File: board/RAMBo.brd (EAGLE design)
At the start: 104.1 x 102.9 mm, 273 parts, among them Q1 PSMN7R0-60YS, Q2 PSMN7R0-60YS, Q3 PSMN7R0-60YS, Q4 IRLML6346TRPBF, Q5 PSMN7R0-60YS, Q8 IRLML6346TRPBF, U1 ATMEGA32U2-MUR, U10 ADUM7441, U2 ATMEGA2560-16AU, U3 TPS54332DDA, U4 AD5206, U5 A4982, U6 A4982, U7 A4982, U8 A4982, U9 A4982, X1 C-GRID-02-70543, X10 C-GRID-04-70543, X11 MSTBV10, X12 SPI, X13 EXT-2, X14 C-GRID-04-70543, X15 C-GRID-04-70543, X16 32u2 EXT, X17 3x2M, X18 3x2M, X2 USB B-TH, X20 M05PTH, X21 C-GRID-03-70543, X22 C-GRID-03-70543, X23 C-GRID-03-70543, X24 C-GRID-03-70543, X25 C-GRID-03-70543, X26 C-GRID-03-70543, X27 C-GRID-02-70543, X28 C-GRID-02-70543, X29 C-GRID-02-70543, X3 C-GRID-02-70543, X30 C-GRID-02-70543, X31 M05PTH, X32 M05PTH, X33 MSTBA6, X34 PWM_EXT, X39 M05X2PTH, X4 C-GRID-04-70543, X40 Analog, X5 C-GRID-02-70543, X6 C-GRID-04-70543, X7 C-GRID-04-70543, X8 C-GRID-04-70543, X9 C-GRID-02-70543, Y1 16MHz KX-7, Y2 16MHz KX-7

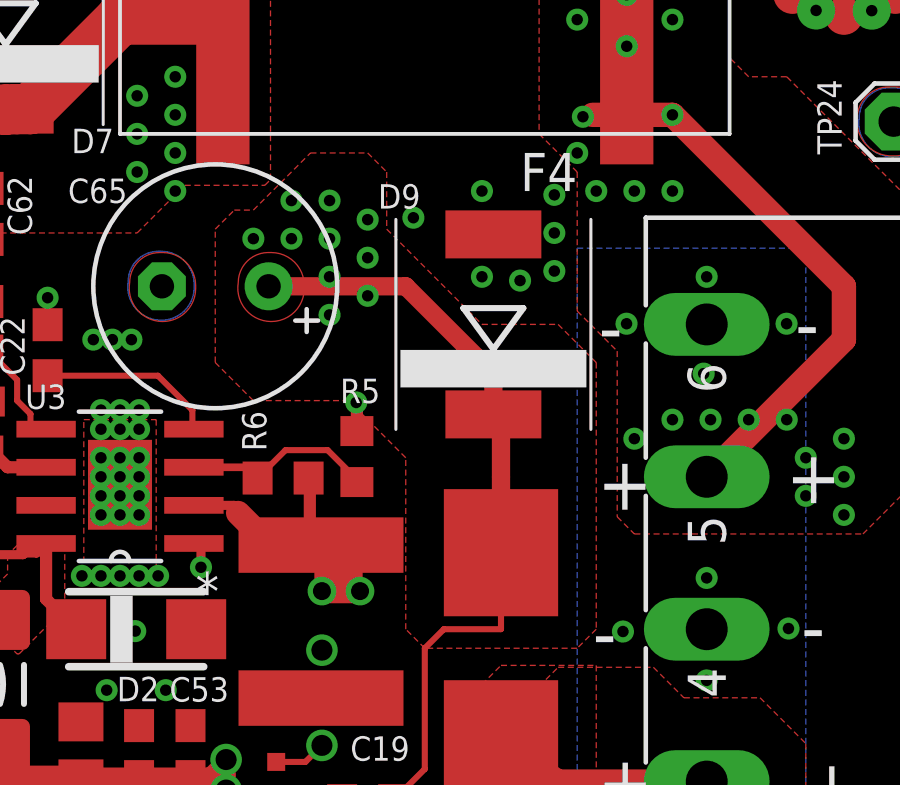
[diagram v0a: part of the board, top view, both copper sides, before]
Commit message: Change SMPS source to mosfet input, diode on this
rail to 27V zener
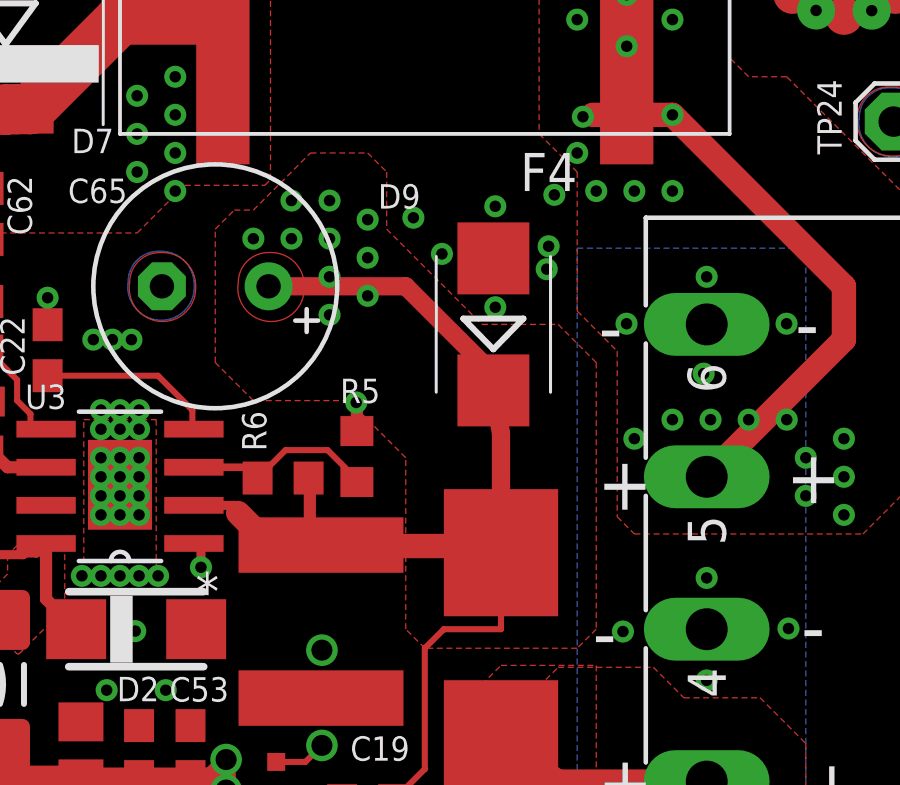
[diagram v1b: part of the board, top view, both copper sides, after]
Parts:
- D9: device ultimachine:DO-214AB -> diode:SMB
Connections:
- net +12V: no longer C19.1, R6.2, U3.2
- net +12V2: now also C19.1, R6.2, U3.2
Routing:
- net +12V: track 179.2 -> 129.2 mm, vias 34 -> 32
- net +12V2: track 137.7 -> 150.6 mm
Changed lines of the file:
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@@
 <layer number="3" name="Route3" color="4" fill="3" visible="no" active="no"/>
 <layer number="14" name="Route14" color="1" fill="6" visible="no" active="no"/>
-<layer number="15" name="15-SUPPLY" color="11" fill="6" visible="no" active="yes"/>
+<layer number="15" name="15-SUPPLY" color="11" fill="6" visible="yes" active="yes"/>
 <layer number="16" name="Bottom" color="1" fill="1" visible="yes" active="yes"/>
 <layer number="17" name="Pads" color="2" fill="1" visible="yes" active="yes"/>
@@
 </class>
 </classes>
-<designrules name="rambo4layer1-2 *">
+<designrules name="rambo4layer1-2">
 <description language="en">&lt;b&gt;EAGLE Design Rules&lt;/b&gt;
 &lt;p&gt;
@@
 <param name="dpGapFactor" value="2.5"/>
 <param name="checkGrid" value="0"/>
-<param name="checkAngle" value="1"/>
+<param name="checkAngle" value="0"/>
 <param name="checkFont" value="1"/>
 <param name="checkRestrict" value="1"/>
@@
 <attribute name="NAME" x="98.656" y="30.281" size="0.8128" layer="25" rot="R90"/>
 </element>
-<element name="D9" library="ultimachine" package="DO-214AB" value="S3A" x="88.646" y="86.36" smashed="yes" rot="R90">
+<element name="D9" library="diode" package="SMB" value="S3A" x="88.646" y="86.36" smashed="yes" rot="R90">
 <attribute name="NAME" x="84.8025" y="90.22" size="0.8128" layer="25"/>
 </element>
@@
 <via x="75.311" y="85.852" extent="1-16" drill="0.381"/>
 <via x="82.931" y="75.5015" extent="1-16" drill="0.7"/>
-<via x="88.265" y="87.9475" extent="1-16" drill="0.381"/>
-<via x="88.265" y="90.805" extent="1-16" drill="0.381"/>
-<via x="90.678" y="89.408" extent="1-16" drill="0.381"/>
+<via x="88.7095" y="86.9315" extent="1-16" drill="0.381"/>
+<via x="88.7095" y="90.297" extent="1-16" drill="0.381"/>
+<via x="90.4875" y="88.9635" extent="1-16" drill="0.381"/>
 <via x="93.085" y="86.3825" extent="1-16" drill="0.381"/>
 <via x="74.6125" y="99.568" extent="1-16" drill="0.381"/>
@@
 <via x="71.755" y="101.9175" extent="1-16" drill="0.381"/>
 <via x="75.565" y="101.9175" extent="1-16" drill="0.381"/>
-<via x="90.678" y="88.138" extent="1-16" drill="0.381"/>
-<via x="89.535" y="87.8205" extent="1-16" drill="0.381"/>
+<via x="86.9315" y="88.7095" extent="1-16" drill="0.381"/>
+<via x="90.424" y="88.2015" extent="1-16" drill="0.381"/>
 <via x="90.678" y="90.678" extent="1-16" drill="0.381"/>
 <via x="85.979" y="89.916" extent="1-16" drill="0.381"/>
@@
 </polygon>
 <contactref element="X30" pad="2"/>
-<contactref element="C19" pad="1"/>
-<contactref element="U3" pad="2"/>
-<contactref element="R6" pad="2"/>
 <contactref element="C27" pad="1"/>
 <contactref element="C32" pad="1"/>
@@
 <via x="18.8595" y="30.48" extent="1-16" drill="0.381"/>
 <wire x1="18.8595" y1="30.48" x2="18.8595" y2="29.425" width="0.4064" layer="1"/>
-<wire x1="82.89925" y1="79.004" x2="82.52825" y2="79.375" width="0.6096" layer="1"/>
-<wire x1="82.52825" y1="79.375" x2="81.661" y2="79.375" width="0.6096" layer="1"/>
-<wire x1="81.661" y1="79.375" x2="80.772" y2="79.4385" width="0.6096" layer="1"/>
-<wire x1="80.772" y1="79.4385" x2="80.137" y2="80.0735" width="0.8128" layer="1"/>
-<wire x1="80.137" y1="80.0735" x2="80.01" y2="80.3275" width="0.3048" layer="1"/>
-<wire x1="80.01" y1="80.3275" x2="78.6638" y2="80.3275" width="0.3048" layer="1"/>
-<wire x1="82.89925" y1="79.004" x2="82.931" y2="78.97225" width="0.508" layer="1"/>
-<wire x1="82.931" y1="78.97225" x2="82.931" y2="77.47" width="0.508" layer="1"/>
-<via x="82.931" y="77.47" extent="1-16" drill="0.6"/>
-<wire x1="92.456" y1="67.5005" x2="92.456" y2="47.371" width="0.508" layer="15"/>
-<wire x1="92.456" y1="47.371" x2="95.25" y2="44.577" width="0.508" layer="15"/>
-<wire x1="95.25" y1="44.577" x2="95.25" y2="43.18" width="0.508" layer="15"/>
 <via x="95.25" y="43.18" extent="1-16" drill="0.6"/>
 <wire x1="96.51" y1="44.44" x2="98.1075" y2="44.44" width="0.508" layer="1"/>
@@
 <wire x1="56.261" y1="18.161" x2="56.261" y2="17.7165" width="0.254" layer="15"/>
 <wire x1="56.261" y1="17.7165" x2="56.3245" y2="17.653" width="0.254" layer="15"/>
-<via x="84.201" y="77.47" extent="1-16" drill="0.6"/>
-<wire x1="84.201" y1="77.47" x2="83.058" y2="77.47" width="0.8128" layer="1"/>
-<wire x1="83.058" y1="77.47" x2="83.2485" y2="77.6605" width="0.8128" layer="1"/>
-<wire x1="83.2485" y1="77.6605" x2="83.2485" y2="78.1685" width="0.8128" layer="1"/>
-<wire x1="82.931" y1="77.47" x2="83.058" y2="77.47" width="0.2032" layer="1"/>
-<wire x1="83.8835" y1="77.6605" x2="83.8835" y2="78.1685" width="0.8128" layer="1"/>
-<polygon width="0.6096" layer="15">
-<vertex x="82.9945" y="77.2795"/>
-<vertex x="84.201" y="77.47"/>
-<vertex x="82.9945" y="77.6605"/>
-</polygon>
-<wire x1="83.8835" y1="77.6605" x2="84.0105" y2="77.6605" width="0.6096" layer="1"/>
-<wire x1="84.0105" y1="77.6605" x2="84.201" y2="77.47" width="0.6096" layer="1"/>
-<wire x1="82.4865" y1="81.23875" x2="82.52825" y2="81.197" width="0.4064" layer="1"/>
-<wire x1="82.52825" y1="81.197" x2="82.52825" y2="79.375" width="0.4064" layer="1"/>
 <contactref element="C61" pad="1"/>
-<wire x1="92.456" y1="67.5005" x2="84.201" y2="75.7555" width="0.508" layer="15"/>
-<wire x1="84.201" y1="75.7555" x2="84.201" y2="77.47" width="0.508" layer="15"/>
 <via x="94.9325" y="46.482" extent="1-16" drill="0.381"/>
 <contactref element="C71" pad="1"/>
@@
 <wire x1="88.9" y1="78.75" x2="88.9" y2="81.28" width="0.6096" layer="1"/>
 <wire x1="88.9" y1="81.28" x2="88.9" y2="82.725" width="0.6096" layer="1"/>
-<wire x1="88.9" y1="82.725" x2="88.646" y2="83.36" width="0.6096" layer="1"/>
-<wire x1="88.646" y1="83.36" x2="88.646" y2="84.709" width="0.6096" layer="1"/>
+<wire x1="88.9" y1="82.725" x2="88.646" y2="84.16" width="0.6096" layer="1"/>
+<wire x1="88.646" y1="84.16" x2="88.646" y2="84.709" width="0.6096" layer="1"/>
 <wire x1="88.646" y1="84.709" x2="85.725" y2="87.63" width="0.6096" layer="1"/>
 <wire x1="85.725" y1="87.63" x2="81.153" y2="87.63" width="0.6096" layer="1"/>
@@
 <wire x1="39.6875" y1="72.644" x2="38.2515" y2="71.208" width="0.2032" layer="1"/>
 <wire x1="38.2515" y1="71.208" x2="37.2745" y2="71.208" width="0.2032" layer="1"/>
+<contactref element="C19" pad="1"/>
+<contactref element="U3" pad="2"/>
+<contactref element="R6" pad="2"/>
+<wire x1="82.89925" y1="79.004" x2="82.52825" y2="79.375" width="0.6096" layer="1"/>
+<wire x1="82.52825" y1="79.375" x2="81.661" y2="79.375" width="0.6096" layer="1"/>
+<wire x1="81.661" y1="79.375" x2="80.772" y2="79.4385" width="0.6096" layer="1"/>
+<wire x1="80.772" y1="79.4385" x2="80.137" y2="80.0735" width="0.8128" layer="1"/>
+<wire x1="80.137" y1="80.0735" x2="80.01" y2="80.3275" width="0.3048" layer="1"/>
+<wire x1="80.01" y1="80.3275" x2="78.6638" y2="80.3275" width="0.3048" layer="1"/>
+<wire x1="82.89925" y1="79.004" x2="82.931" y2="78.97225" width="0.508" layer="1"/>
+<wire x1="82.4865" y1="81.23875" x2="82.52825" y2="81.197" width="0.4064" layer="1"/>
+<wire x1="82.52825" y1="81.197" x2="82.52825" y2="79.375" width="0.4064" layer="1"/>
+<wire x1="82.931" y1="78.97225" x2="88.9" y2="78.97225" width="0.8128" layer="1"/>
+<wire x1="88.9" y1="78.97225" x2="88.9" y2="78.75" width="0.8128" layer="1"/>
 </signal>
 <signal name="N$86">

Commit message: set L2 part
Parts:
- D9: value S3A -> 1SMB5935BT3G
- L2: value (none) -> CBC2012T100M
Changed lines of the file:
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@@
 <attribute name="NAME" x="98.656" y="30.281" size="0.8128" layer="25" rot="R90"/>
 </element>
-<element name="D9" library="diode" package="SMB" value="S3A" x="88.646" y="86.36" smashed="yes" rot="R90">
+<element name="D9" library="diode" package="SMB" value="1SMB5935BT3G" x="88.646" y="86.36" smashed="yes" rot="R90">
 <attribute name="NAME" x="84.8025" y="90.22" size="0.8128" layer="25"/>
 </element>
@@
 <attribute name="VALUE" x="71.1835" y="50.9905" size="1.27" layer="27" rot="R90"/>
 </element>
-<element name="L2" library="resistor" package="C0805" value="" x="64.008" y="68.6435" smashed="yes">
+<element name="L2" library="resistor" package="C0805" value="CBC2012T100M" x="64.008" y="68.6435" smashed="yes">
 <attribute name="NAME" x="60.8965" y="67.8815" size="0.8128" layer="25"/>
 <attribute name="VALUE" x="63.119" y="66.3575" size="1.27" layer="27"/>
@@
 <wire x1="36.1315" y1="56.3635" x2="35.98" y2="56.515" width="0.2032" layer="1"/>
 <via x="79.73675" y="70.83875" extent="1-16" drill="0.7"/>
-<via x="79.73675" y="71.85475" extent="1-16" drill="0.7"/>
+<via x="79.73675" y="71.85475" extent="1-16" drill="0.5"/>
 <wire x1="78.5495" y1="71.286" x2="78.6545" y2="71.286" width="0.6096" layer="1"/>
 <wire x1="78.6545" y1="71.286" x2="79.73675" y2="70.83875" width="0.6096" layer="1"/>

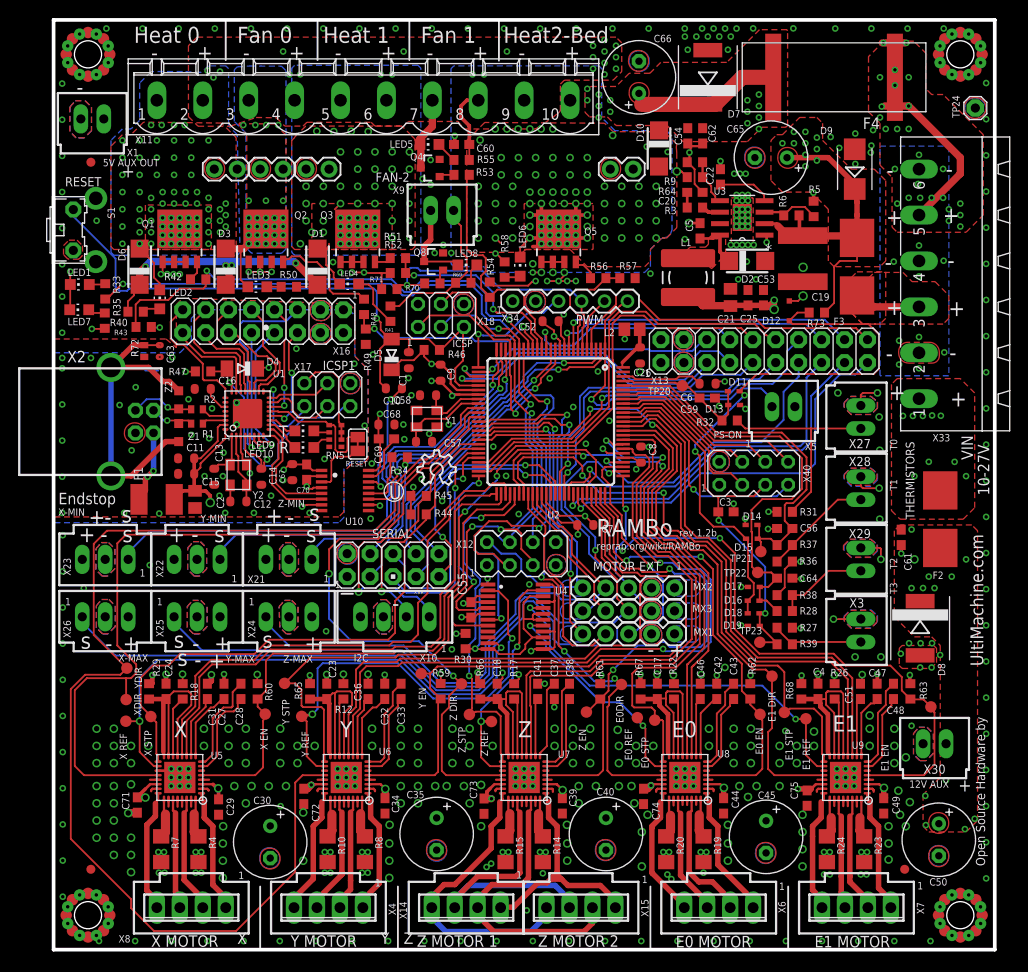
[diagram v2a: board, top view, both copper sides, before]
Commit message: consolidate V-mot bulk caps to 1 470uF, move
thermistor connectors, move PS-ON connector, add jumper to disable SMPS,
adjust bulk cap placement on V-heat, misc layout and silk improvements
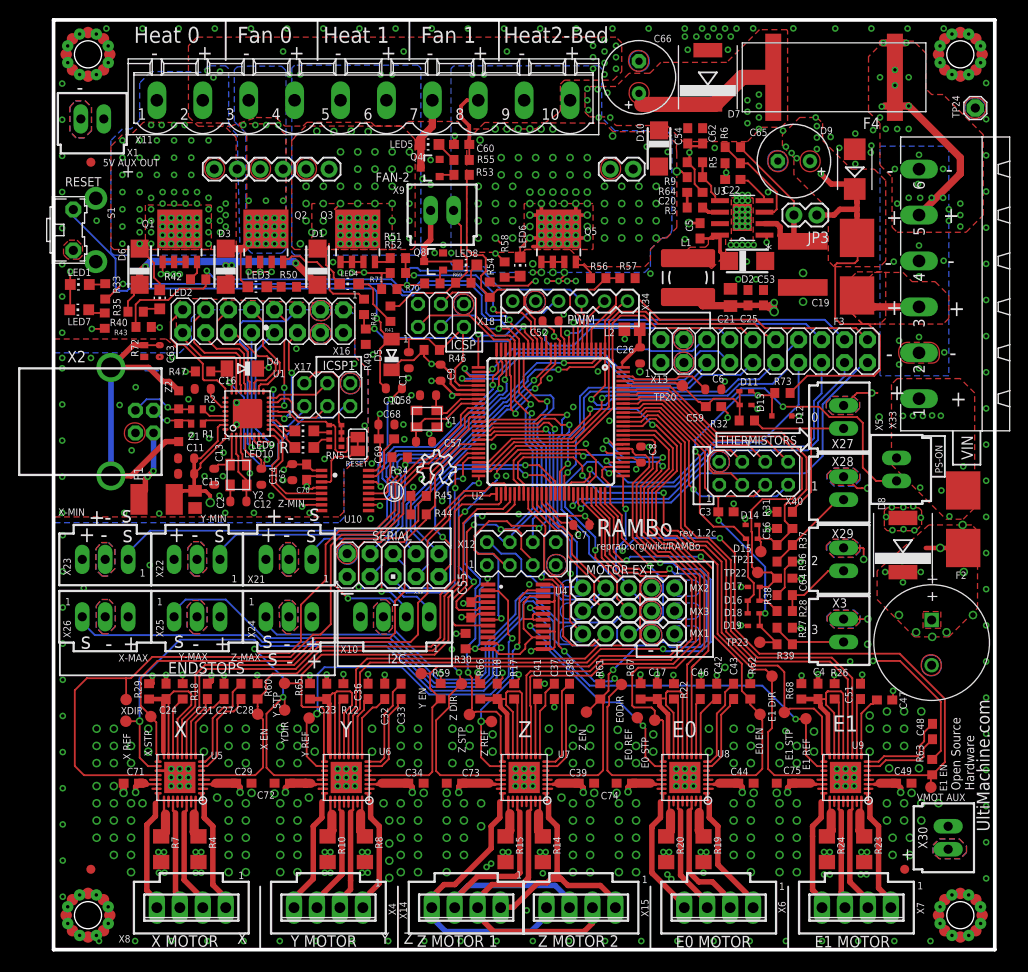
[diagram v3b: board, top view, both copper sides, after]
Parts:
- removed C30, C35, C40, C45, C50: 100uF, resistor:E3,5-8
- removed C61: 100nF, rcl:C0603
- added C76: (no value), resistor:C12,5-5
- added JP3: (no value), SparkFun:1X02
- moved TP0 18.1 mm to (25.6, 26.5)
- moved X5 14.3 mm to (93.3, 53.1), turned to 90 degrees
- moved D12 11.6 mm to (80.6, 59.1), turned to 0 degrees
- moved X30 10.5 mm to (99.0, 12.4), turned to 270 degrees
- moved R5 10.3 mm to (75.1, 87.0), turned to 0 degrees
- moved R6 9.95 mm to (75.2, 88.8)
- moved R73 9.67 mm to (80.6, 61.6)
- moved D8 9.40 mm to (94.0, 44.8), turned to 90 degrees
- moved TP18 8.89 mm to (97.1, 18.0)
- moved R63 8.72 mm to (97.2, 20.2)
- moved C48 6.20 mm to (97.3, 24.1)
- moved C34 4.25 mm to (40.1, 18.4), turned to 0 degrees
- moved C73 4.14 mm to (44.4, 18.4), turned to 180 degrees
- moved C29 3.84 mm to (21.1, 18.4), turned to 0 degrees
- moved C39 3.66 mm to (59.0, 18.4), turned to 0 degrees
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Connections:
- new net N$111: C19.1, JP3.2, R6.2, U3.2
- net +12V: now also C76.+; no longer C30.+, C35.+, C40.+, C45.+, C50.+, C61.1
- net +12V2: now also JP3.1; no longer C19.1, R6.2, U3.2
- net GND: now also C76.-; no longer C30.-, C35.-, C40.-, C45.-, C50.-, C61.2
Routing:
- net Y-DIR: track 136.0 -> 66.8 mm, vias 0 -> 2
- net +12V: track 129.2 -> 66.5 mm, vias 32 -> 27
- net OVREF: track 64.7 -> 37.9 mm
- net PG5: track 35.0 -> 54.6 mm, vias 1 -> 2
- net N$111: track 0.00 -> 19.5 mm
- net VCC: track 79.7 -> 97.8 mm
- net +12V2: track 150.6 -> 158.9 mm, vias 36 -> 35
- net X-DIR: track 91.7 -> 85.3 mm
- net N$97: track 6.52 -> 11.2 mm
- net E1-EN: track 69.7 -> 73.6 mm
- net N$87: track 24.1 -> 20.3 mm
- net N$94: track 5.96 -> 3.86 mm
- net X-REF: track 60.3 -> 62.3 mm
- net Y-REF: track 49.1 -> 47.1 mm
- net N$91: track 10.4 -> 8.54 mm
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- added copper zone on layer 1, net N$112
- removed copper zone on layer 15, net N$10
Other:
- board text added: "0"
- board text added: "2"
- board text added: "3"
- board text added: "ENDSTOPS"
- board text added: "Open Source Hardware"
- board text added: "VMOT AUX"
- board text added: "rev 1.2c"
- board text removed: "10-27V"
- board text removed: "12V AUX"
- board text removed: "Endstop"
- board text removed: "Open Source Hardware by"
- board text removed: "T0"
- board text removed: "T1"
- board text removed: "T2"
- board text removed: "T3"
- board text removed: "rev 1.2b"

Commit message: remove solder thieving, shrink through pads to
improve wave, new stackup, fix some trace angles, improve stepper
layout, silk screen fixes,
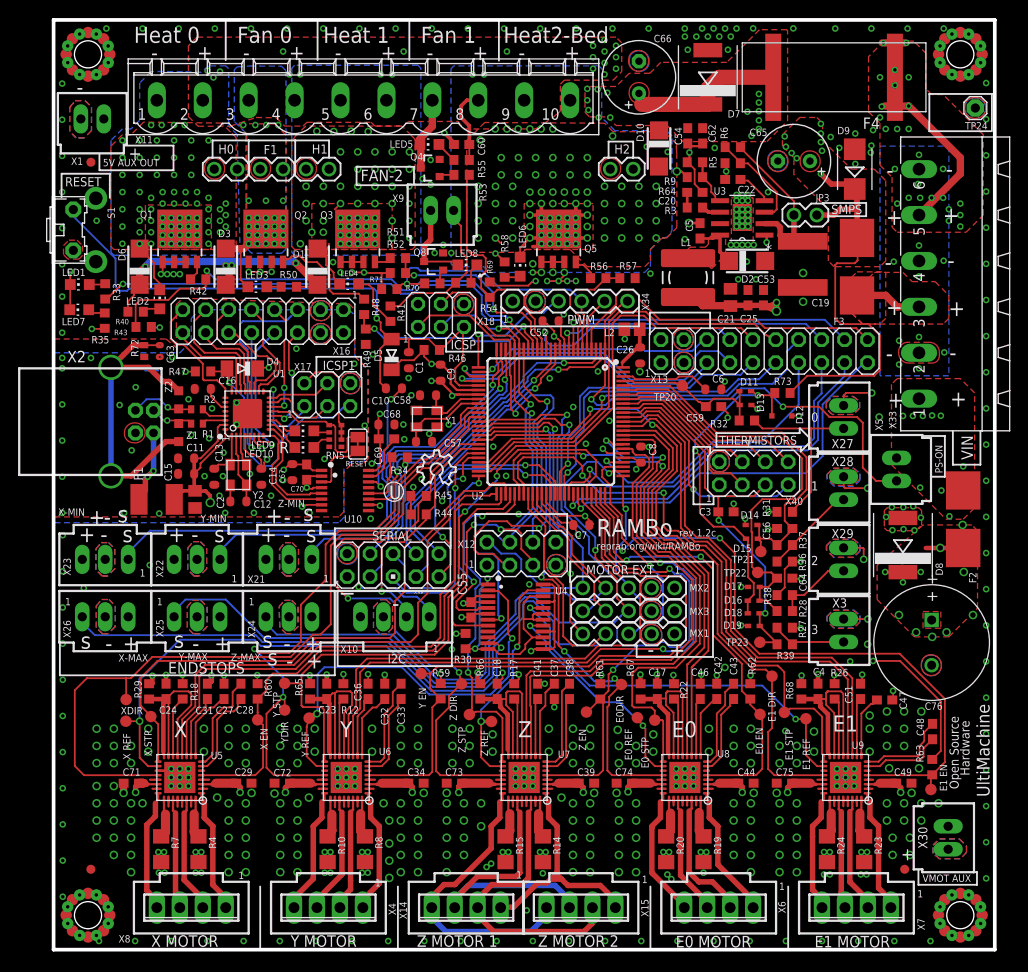
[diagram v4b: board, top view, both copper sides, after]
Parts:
- C76: value (none) -> 470uF
- moved TP4 0.64 mm to (22.6, 25.4)
- moved TP18 0.25 mm to (97.1, 17.7)
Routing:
- net Z-EN: track 58.8 -> 55.0 mm
- net Y-MS1: track 80.4 -> 76.6 mm
- net VCC: track 97.8 -> 96.4 mm
- net RESET2: track 30.1 -> 28.9 mm
- net +12V3: track 56.3 -> 57.4 mm
- net +12V2: track 158.9 -> 158.0 mm
- net E1-REF: track 45.5 -> 45.0 mm
- removed copper zone on layer 16, net PL3
- removed copper zone on layer 16, net PL4
- removed copper zone on layer 16, net PL5
- removed copper zone on layer 16, net VCC
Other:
- board text added: "F1"
- board text added: "H0"
- board text added: "H1"
- board text added: "H2"
- board text added: "Hardware"
- board text added: "Open Source"
- board text added: "SMPS"
- board text added: "Stack Up GTO ------ Top Silk GTS - Solder Mask GTL------------ 2oz 0.61mm G2L ----------- 1oz 0.1mm G3L ----------- 1oz 0.61mm GBL ----------- 2oz GBS - Solder Mask Total Thickness ~ 1.62mm"
- board text added: "UltiMachine"
- board text removed: "Open Source Hardware"
- board text removed: "Stack Up GTO ------ Top Silk GTS - Solder Mask GTL------------ 1oz 0.61mm G2L ----------- 2oz 0.2mm G3L ----------- 2oz 0.61mm GBL ----------- 1oz GBS - Solder Mask Total Thickness ~ 1.62mm"
- board text removed: "UltiMachine.com"
